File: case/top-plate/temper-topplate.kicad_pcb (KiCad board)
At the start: 2 copper layers, 111.4 x 90 mm, 18 parts, among them SW10 SW_PUSH, SW11 SW_PUSH, SW12 SW_PUSH, SW14 SW_PUSH, SW15 SW_PUSH, SW16 SW_PUSH, SW17 SW_PUSH, SW18 SW_PUSH, SW19 SW_PUSH, SW2 SW_PUSH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

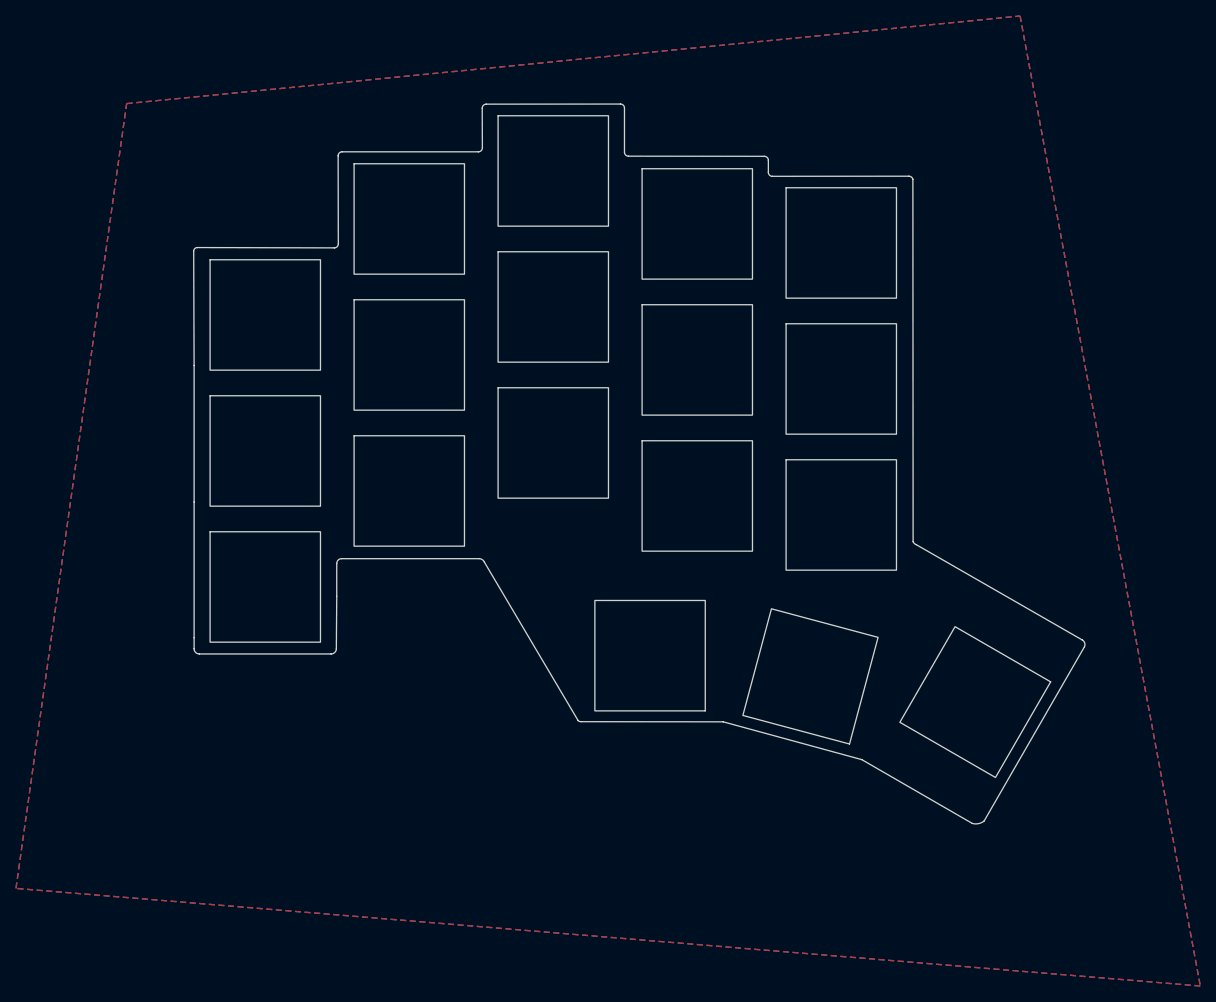
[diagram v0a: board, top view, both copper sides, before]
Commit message: Convert switches to Choc v2 sockets
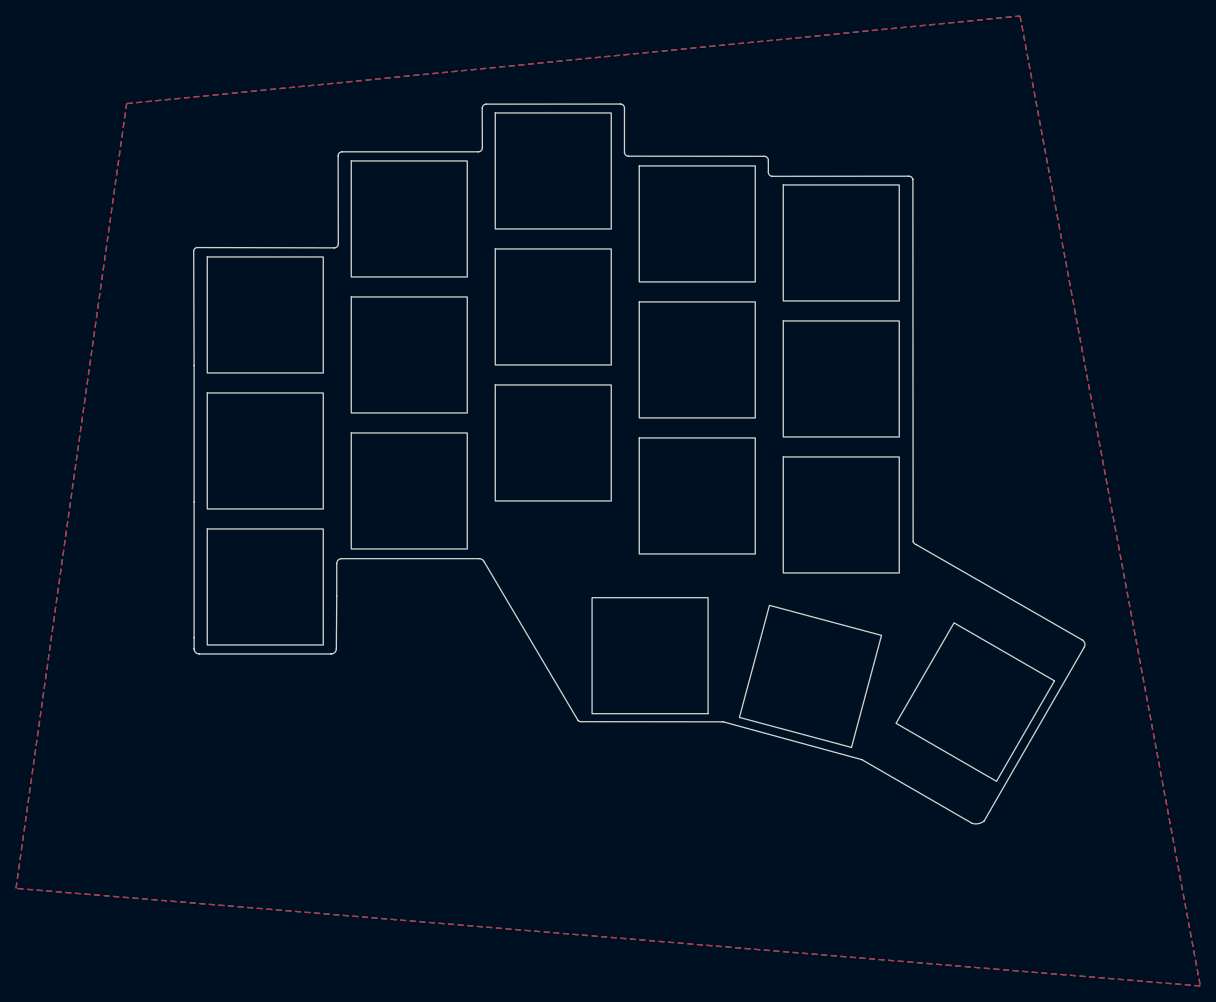
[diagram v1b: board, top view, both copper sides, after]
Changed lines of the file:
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@@
 		)
 		(fp_rect
-			(start -6.9 -6.9)
-			(end 6.9 6.9)
+			(start -7.25 -7.25)
+			(end 7.25 7.25)
 			(stroke
 				(width 0.12)
@@
 		)
 		(fp_rect
-			(start -6.9 -6.9)
-			(end 6.9 6.9)
+			(start -7.25 -7.25)
+			(end 7.25 7.25)
 			(stroke
 				(width 0.12)
@@
 		)
 		(fp_rect
-			(start -6.9 -6.9)
-			(end 6.9 6.9)
+			(start -7.25 -7.25)
+			(end 7.25 7.25)
 			(stroke
 				(width 0.12)
@@
 		)
 		(fp_rect
-			(start -6.9 -6.9)
-			(end 6.9 6.9)
+			(start -7.25 -7.25)
+			(end 7.25 7.25)
 			(stroke
 				(width 0.12)
@@
 		)
 		(fp_rect
-			(start -6.9 -6.9)
-			(end 6.9 6.9)
+			(start -7.25 -7.25)
+			(end 7.25 7.25)
 			(stroke
 				(width 0.12)
@@
 		)
 		(fp_rect
-			(start -6.9 -6.9)
-			(end 6.9 6.9)
+			(start -7.25 -7.25)
+			(end 7.25 7.25)
 			(stroke
 				(width 0.12)
@@
 		)
 		(fp_rect
-			(start -6.9 -6.9)
-			(end 6.9 6.9)
+			(start -7.25 -7.25)
+			(end 7.25 7.25)
 			(stroke
 				(width 0.12)
@@
 		)
 		(fp_rect
-			(start -6.9 -6.9)
-			(end 6.9 6.9)
+			(start -7.25 -7.25)
+			(end 7.25 7.25)
 			(stroke
 				(width 0.12)
@@
 		)
 		(fp_rect
-			(start -6.9 -6.9)
-			(end 6.9 6.9)
+			(start -7.25 -7.25)
+			(end 7.25 7.25)
 			(stroke
 				(width 0.12)
@@
 		)
 		(fp_rect
-			(start -6.9 -6.9)
-			(end 6.9 6.9)
+			(start -7.25 -7.25)
+			(end 7.25 7.25)
 			(stroke
 				(width 0.12)
@@
 		)
 		(fp_rect
-			(start -6.9 -6.9)
-			(end 6.9 6.9)
+			(start -7.25 -7.25)
+			(end 7.25 7.25)
 			(stroke
 				(width 0.12)
@@
 		)
 		(fp_rect
-			(start -6.9 -6.9)
-			(end 6.9 6.9)
+			(start -7.25 -7.25)
+			(end 7.25 7.25)
 			(stroke
 				(width 0.12)
@@
 		)
 		(fp_rect
-			(start -6.9 -6.9)
-			(end 6.9 6.9)
+			(start -7.25 -7.25)
+			(end 7.25 7.25)
 			(stroke
 				(width 0.12)
@@
 		)
 		(fp_rect
-			(start -6.9 -6.9)
-			(end 6.9 6.9)
+			(start -7.25 -7.25)
+			(end 7.25 7.25)
 			(stroke
 				(width 0.12)
@@
 		)
 		(fp_rect
-			(start -6.9 -6.9)
-			(end 6.9 6.9)
+			(start -7.25 -7.25)
+			(end 7.25 7.25)
 			(stroke
 				(width 0.12)
@@
 		)
 		(fp_rect
-			(start -6.9 -6.9)
-			(end 6.9 6.9)
+			(start -7.25 -7.25)
+			(end 7.25 7.25)
 			(stroke
 				(width 0.12)
@@
 		(fp_poly
 			(pts
-				(xy -6.9 -6.9) (xy 6.9 -6.9) (xy 6.9 6.9) (xy -6.9 6.9)
+				(xy -7.25 -7.25) (xy 7.25 -7.25) (xy 7.25 7.25) (xy -7.25 7.25)
 			)
 			(stroke
@@
 		(fp_poly
 			(pts
-				(xy -6.9 -6.9) (xy 6.9 -6.9) (xy 6.9 6.9) (xy -6.9 6.9)
-			)
-			(stroke
+				(xy -7.25 -7.25) (xy 7.25 -7.25) (xy 7.25 7.25) (xy -7.25 7.25)
+			)
+			(stroke
